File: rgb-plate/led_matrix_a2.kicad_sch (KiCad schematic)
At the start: 64 parts

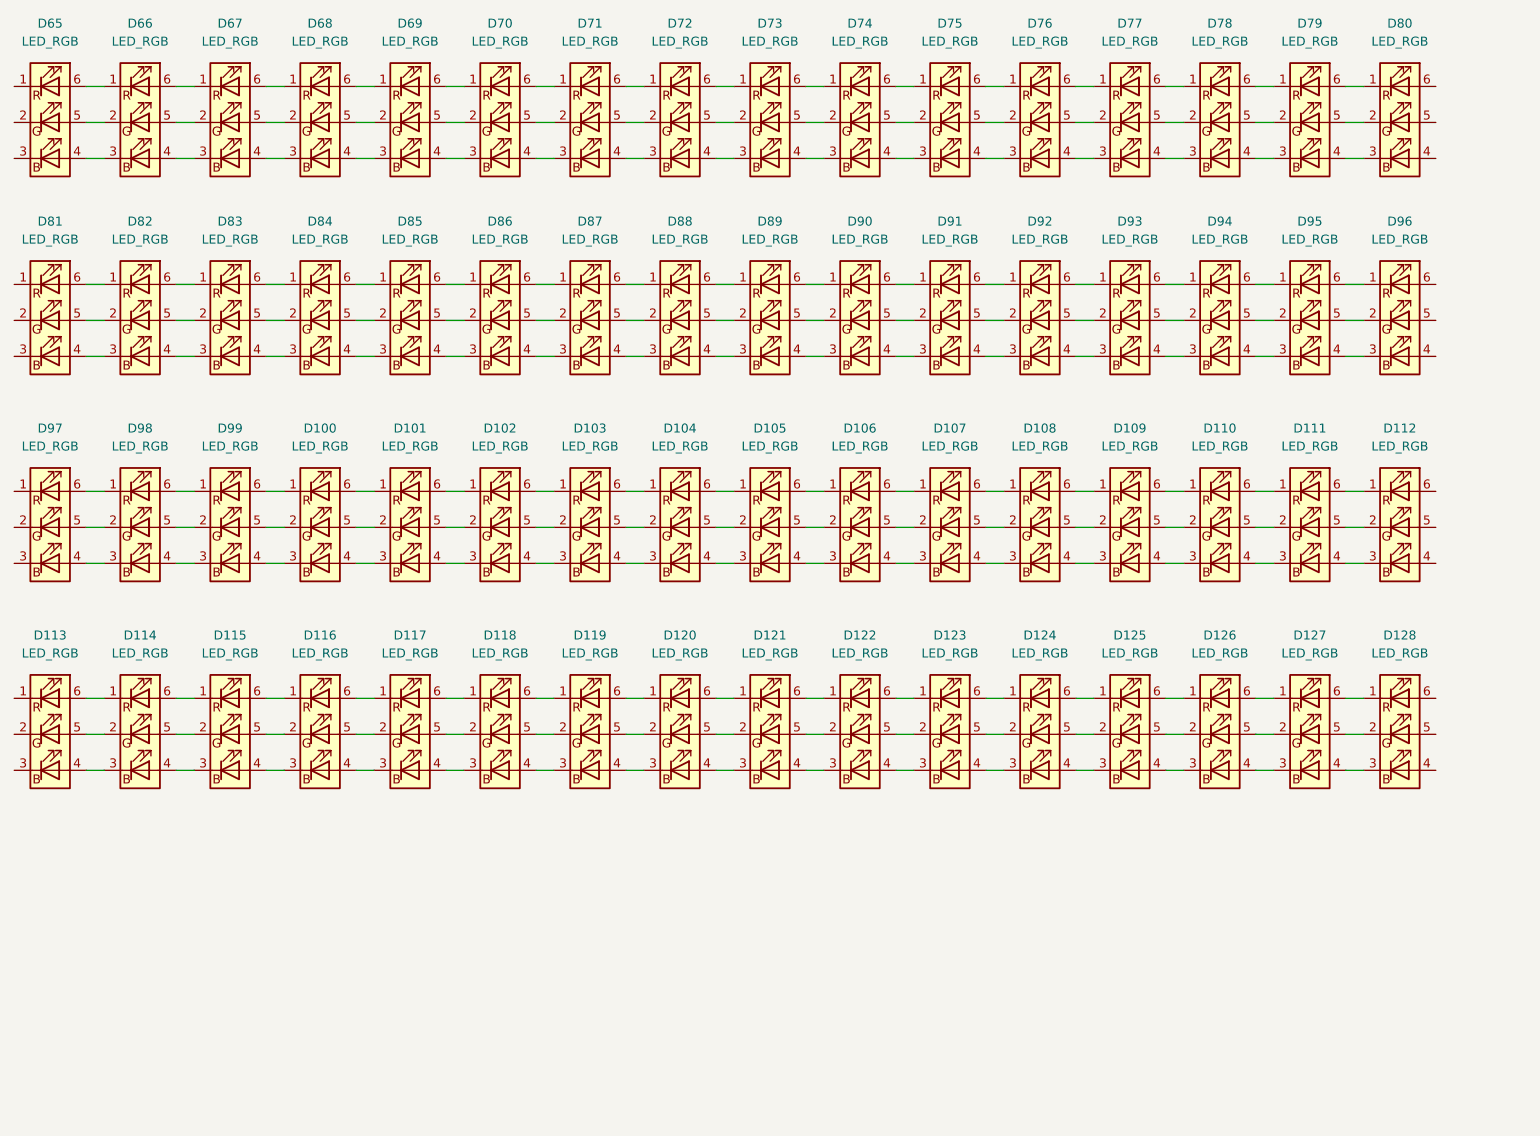
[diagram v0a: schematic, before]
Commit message: initial layout on single board, may need to split up
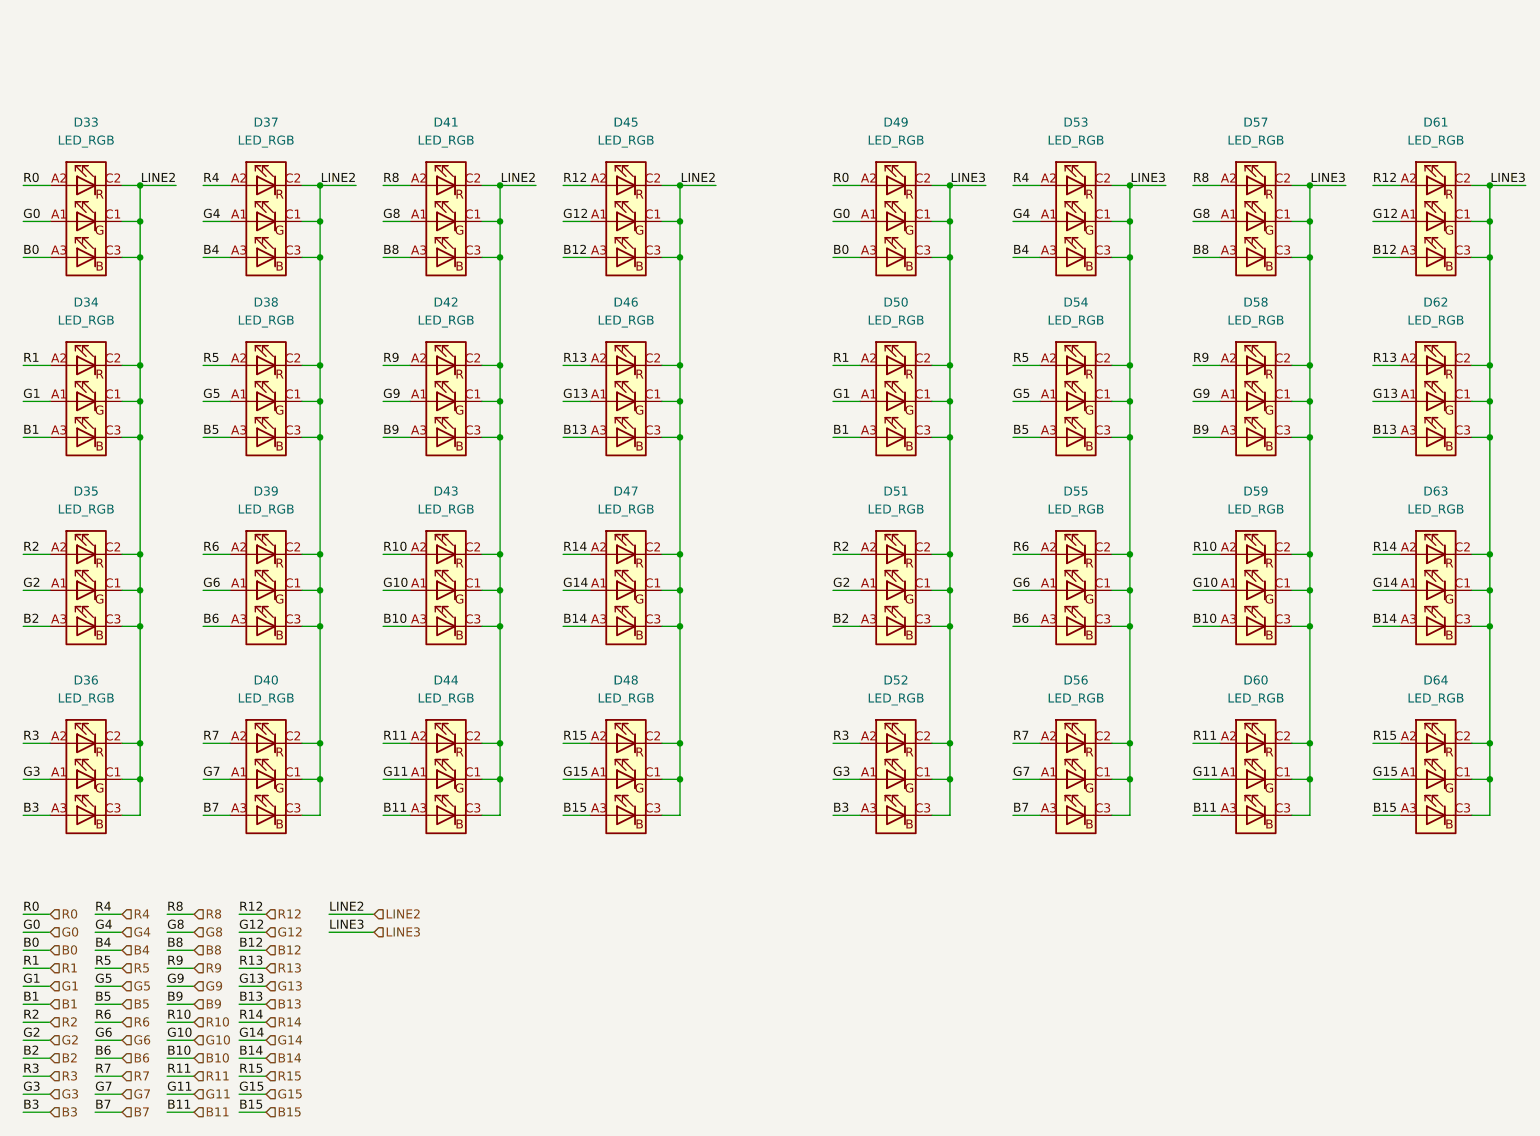
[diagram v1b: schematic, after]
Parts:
- removed D100, D101, D102, D103, D104, D105, D106, D107, D108, D109, D110, D111, D112, D113, D114, D115, D116, D117, D118, D119, D120, D121, D122, D123, D124, D125, D126, D127, D128, D65, D66, D67, D68, D69, D70, D71, D72, D73, D74, D75, D76, D77, D78, D79, D80, D81, D82, D83, D84, D85, D86, D87, D88, D89, D90, D91, D92, D93, D94, D95, D96, D97, D98, D99: LED_RGB, symbol Device:LED_RGB
- added D33, D34, D35, D36, D37, D38, D39, D40, D41, D42, D43, D44, D45, D46, D47, D48, D49, D50, D51, D52, D53, D54, D55, D56, D57, D58, D59, D60, D61, D62, D63, D64: LED_RGB, LRTBGVSR-4U4V-JW+8A8B-D8-3S4U-7Z:LRTBGVSR4U4VJW8A8BD83S4U7Z, symbol LRTBGVSR-4U4V-JW+8A8B-D8-3S4U-:LED_RGB
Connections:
- new net B0: D33.A3 (BA), D49.A3 (BA)
- new net B1: D34.A3 (BA), D50.A3 (BA)
- new net B10: D43.A3 (BA), D59.A3 (BA)
- new net B11: D44.A3 (BA), D60.A3 (BA)
- new net B12: D45.A3 (BA), D61.A3 (BA)
- new net B13: D46.A3 (BA), D62.A3 (BA)
- new net B14: D47.A3 (BA), D63.A3 (BA)
- new net B15: D48.A3 (BA), D64.A3 (BA)
- new net B2: D35.A3 (BA), D51.A3 (BA)
- new net B3: D36.A3 (BA), D52.A3 (BA)
- new net B4: D37.A3 (BA), D53.A3 (BA)
- new net B5: D38.A3 (BA), D54.A3 (BA)
- new net B6: D39.A3 (BA), D55.A3 (BA)
- new net B7: D40.A3 (BA), D56.A3 (BA)
- new net B8: D41.A3 (BA), D57.A3 (BA)
- new net B9: D42.A3 (BA), D58.A3 (BA)
- new net G0: D33.A1 (GA), D49.A1 (GA)
- new net G1: D34.A1 (GA), D50.A1 (GA)
- new net G10: D43.A1 (GA), D59.A1 (GA)
- new net G11: D44.A1 (GA), D60.A1 (GA)
- new net G12: D45.A1 (GA), D61.A1 (GA)
- new net G13: D46.A1 (GA), D62.A1 (GA)
- new net G14: D47.A1 (GA), D63.A1 (GA)
- new net G15: D48.A1 (GA), D64.A1 (GA)
- new net G2: D35.A1 (GA), D51.A1 (GA)
- new net G3: D36.A1 (GA), D52.A1 (GA)
- new net G4: D37.A1 (GA), D53.A1 (GA)
- new net G5: D38.A1 (GA), D54.A1 (GA)
- new net G6: D39.A1 (GA), D55.A1 (GA)
- new net G7: D40.A1 (GA), D56.A1 (GA)
- new net G8: D41.A1 (GA), D57.A1 (GA)
- new net G9: D42.A1 (GA), D58.A1 (GA)
- new net LINE2: D33.C1 (GK), D33.C2 (RK), D33.C3 (BK), D34.C1 (GK), D34.C2 (RK), D34.C3 (BK), D35.C1 (GK), D35.C2 (RK), D35.C3 (BK), D36.C1 (GK), D36.C2 (RK), D36.C3 (BK), D37.C1 (GK), D37.C2 (RK), D37.C3 (BK), D38.C1 (GK), D38.C2 (RK), D38.C3 (BK), D39.C1 (GK), D39.C2 (RK), D39.C3 (BK), D40.C1 (GK), D40.C2 (RK), D40.C3 (BK), D41.C1 (GK), D41.C2 (RK), D41.C3 (BK), D42.C1 (GK), D42.C2 (RK), D42.C3 (BK), D43.C1 (GK), D43.C2 (RK), D43.C3 (BK), D44.C1 (GK), D44.C2 (RK), D44.C3 (BK), D45.C1 (GK), D45.C2 (RK), D45.C3 (BK), D46.C1 (GK), D46.C2 (RK), D46.C3 (BK), D47.C1 (GK), D47.C2 (RK), D47.C3 (BK), D48.C1 (GK), D48.C2 (RK), D48.C3 (BK)
- new net LINE3: D49.C1 (GK), D49.C2 (RK), D49.C3 (BK), D50.C1 (GK), D50.C2 (RK), D50.C3 (BK), D51.C1 (GK), D51.C2 (RK), D51.C3 (BK), D52.C1 (GK), D52.C2 (RK), D52.C3 (BK), D53.C1 (GK), D53.C2 (RK), D53.C3 (BK), D54.C1 (GK), D54.C2 (RK), D54.C3 (BK), D55.C1 (GK), D55.C2 (RK), D55.C3 (BK), D56.C1 (GK), D56.C2 (RK), D56.C3 (BK), D57.C1 (GK), D57.C2 (RK), D57.C3 (BK), D58.C1 (GK), D58.C2 (RK), D58.C3 (BK), D59.C1 (GK), D59.C2 (RK), D59.C3 (BK), D60.C1 (GK), D60.C2 (RK), D60.C3 (BK), D61.C1 (GK), D61.C2 (RK), D61.C3 (BK), D62.C1 (GK), D62.C2 (RK), D62.C3 (BK), D63.C1 (GK), D63.C2 (RK), D63.C3 (BK), D64.C1 (GK), D64.C2 (RK), D64.C3 (BK)
- new net R0: D33.A2 (RA), D49.A2 (RA)
- new net R1: D34.A2 (RA), D50.A2 (RA)
- new net R10: D43.A2 (RA), D59.A2 (RA)
- new net R11: D44.A2 (RA), D60.A2 (RA)
- new net R12: D45.A2 (RA), D61.A2 (RA)
- new net R13: D46.A2 (RA), D62.A2 (RA)
- new net R14: D47.A2 (RA), D63.A2 (RA)
- new net R15: D48.A2 (RA), D64.A2 (RA)
- new net R2: D35.A2 (RA), D51.A2 (RA)
- new net R3: D36.A2 (RA), D52.A2 (RA)
- new net R4: D37.A2 (RA), D53.A2 (RA)
- new net R5: D38.A2 (RA), D54.A2 (RA)
- new net R6: D39.A2 (RA), D55.A2 (RA)
- new net R7: D40.A2 (RA), D56.A2 (RA)
- new net R8: D41.A2 (RA), D57.A2 (RA)
- new net R9: D42.A2 (RA), D58.A2 (RA)
